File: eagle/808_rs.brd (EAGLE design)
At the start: 100 x 80 mm, 82 parts, among them IC1 TL072P, IC2 TL072P, Q74 MPF102, SW1_A LSP11, SW1_B LSP11, SW1_C LSP11, SW2_A LSP11, SW2_B LSP11, SW2_C LSP11

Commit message: gcode with well separated traces
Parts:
- moved ACCENT 4.33 mm to (21.1, 49.3)
- moved C111 3.31 mm to (18.3, 30.2), turned to 270 degrees
- moved R297 1.52 mm to (18.8, 49.5)
- moved SW1_C 1.44 mm to (75.9, 72.1)
- moved SW1_B 1.37 mm to (81.8, 35.6)
- moved SW2_C 0.92 mm to (82.0, 42.4)
- moved R323 0.92 mm to (77.0, 59.2)
- moved R324 0.80 mm to (76.7, 67.6)
- moved R330 0.80 mm to (85.9, 67.6)
- moved U$1 0.57 mm to (40.1, 9.14)
- moved D63 0.51 mm to (57.9, 57.1)
- moved R325 0.51 mm to (66.0, 51.6)
- moved D64 0.25 mm to (36.8, 46.7)
- moved C114 0.25 mm to (19.3, 36.8)
- moved R303 0.25 mm to (39.4, 52.3)
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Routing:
- net N$351: track 319.1 -> 324.5 mm
- net N$4: track 12.5 -> 8.40 mm
- net N$348: track 59.1 -> 62.1 mm
- net -12V: track 323.6 -> 325.9 mm
- net N$163: track 62.0 -> 64.2 mm
- net N$345: track 3.81 -> 2.59 mm
- net RS: track 2.54 -> 3.61 mm
- net N$167: track 64.0 -> 63.1 mm
- net N$473: track 3.07 -> 2.18 mm
- net N$336: track 15.5 -> 14.7 mm
- net N$170: track 73.2 -> 73.9 mm
- net GND: track 357.2 -> 358.0 mm
- net N$318: track 23.7 -> 24.4 mm
- net N$172: track 19.7 -> 19.0 mm
- net N$357: track 86.0 -> 86.7 mm
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
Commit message: schematic updated
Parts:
- removed C5: 0.1uF, TR808clone:C035-025X75
- removed D1: 1N4148DO35-7, TR808clone:DO35-7
- removed R1: 22K, TR808clone:0207/5V
- removed R295: 1K, TR808clone:0207/5V
- removed SW1_A, SW1_B, SW1_C, SW2_A, SW2_B, SW2_C: LSP11, solpad:LSP11
- added OUT_NORM: 22-23-2021, con-molex:22-23-2021
- added R238: 1K, TR808clone:0207/7
- added SW8: 808_LT_MSS42_SW_4PDT, 808_lt:808_LT_MSS42_SW_SLIDE
- OUTPUT: value LSP11 -> AUDIO-JACK; device solpad:LSP11 -> erthenvar:ERTHENVAR-JACK-90DEG
- Q59, Q61, Q62, Q63: value (none) -> 2N3904; device transistor:TO92-CBE -> 808_lt:TO92
- Q60: value (none) -> 2N3906; device transistor:TO92-EBC -> 808_lt:TO92
- moved OUTPUT 125.8 mm to (1.78, -45.0)
- moved ACCENT 23.1 mm to (20.3, 72.4)
- moved TRIGGER 23.1 mm to (21.1, 49.3)
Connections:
- removed net N$345: R319.2, SW1_B.MP
- removed net N$473: R324.1, SW1_C.MP
- removed net RS_CL_OUT: OUTPUT.MP, R295.1
- new net LT_LC_OUT: OUTPUT.P$3, R238.1
- new net N$7: C125.P$1, SW8.P$11
- net +12V: now also Q63.1; no longer Q63.C
- net -12V: now also Q61.3; no longer Q61.E
- net GND: now also OUTPUT.P$1, OUT_NORM.2, Q59.3, Q62.3; no longer Q59.E, Q62.E, R1.1
- net N$161: now also Q61.1; no longer Q61.C
- net N$163: now also Q61.2; no longer Q61.B
- net N$165: now also SW8.P$3; no longer SW2_B.MP
- net N$170: now also R238.2; no longer R295.2
- net N$172: now also Q62.1; no longer Q62.C
- net N$174: now also Q62.2; no longer Q62.B
- net N$2: now also R319.2, SW8.P$10; no longer C125.P$1, SW1_A.MP
- net N$306: now also SW8.P$1; no longer SW2_C.MP
- net N$317: now also Q60.2; no longer Q60.B
- net N$318: now also Q59.2; no longer Q59.B
- net N$319: now also Q59.1; no longer Q59.C
- net N$329: now also Q63.2; no longer Q63.B
- net N$330: now also Q63.3; no longer Q63.E
- net N$338: now also SW8.P$2; no longer SW2_A.MP
- net N$357: now also Q60.1; no longer Q60.C
- net N$5: now also OUTPUT.P$2, OUT_NORM.1; no longer D1.A, TRIGGER.MP
- net N$6: now also R324.1, SW8.P$12; no longer C5.P$1, D1.C, R1.2
- net RS: now also TRIGGER.MP, U$1.15, U$1.16; no longer ACCENT.MP
- net TRIG: now also ACCENT.MP, Q60.3, U$1.13, U$1.14; no longer C5.P$2, Q60.E
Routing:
- net N$6: track 10.7 -> 0.00 mm
- net RS_CL_OUT: track 8.89 -> 0.00 mm
- net GND: track 358.0 -> 364.8 mm
- net N$317: track 13.8 -> 19.5 mm
- net -12V: track 325.9 -> 331.2 mm
- net TRIG: track 12.6 -> 7.62 mm
- net N$161: track 67.4 -> 72.3 mm
- net N$5: track 4.86 -> 0.00 mm
- net N$170: track 73.9 -> 69.3 mm
- net N$319: track 4.31 -> 8.08 mm
- net N$172: track 19.0 -> 22.8 mm
- net +12V: track 132.2 -> 136.0 mm
- net N$2: track 3.27 -> 0.00 mm
- net N$329: track 24.8 -> 28.0 mm
- net N$345: track 2.59 -> 0.00 mm
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
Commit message: 2sk30
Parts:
- removed Q74: MPF102, mes_transistors:TO92F
- added Q1: 2SK30, 808:TO92
- moved R330 171.8 mm to (-85.1, 85.1), turned to 0 degrees
- moved R326 169.6 mm to (-69.8, 85.1)
- moved R318 167.9 mm to (-85.1, 78.7), turned to 0 degrees
- moved R327 157.7 mm to (-77.5, 85.1), turned to 0 degrees
- moved Q62 147.8 mm to (-80.0, 90.2), turned to 0 degrees
- moved R316 143.2 mm to (-69.8, 78.7), turned to 0 degrees
- moved R317 143.1 mm to (-77.5, 78.7), turned to 0 degrees
- moved R314 140.4 mm to (-54.6, 78.7), turned to 0 degrees
- moved C117 138.7 mm to (-76.2, 40.6), turned to 0 degrees
- moved C116 134.8 mm to (-69.8, 40.6), turned to 0 degrees
- moved C126 132.6 mm to (-34.3, 66.0)
- moved R325 132.6 mm to (-62.2, 85.1), turned to 0 degrees
- moved R324 132.5 mm to (-54.6, 85.1), turned to 0 degrees
- moved R313 128.9 mm to (-47.0, 78.7), turned to 0 degrees
- moved R323 126.6 mm to (-47.0, 85.1), turned to 0 degrees
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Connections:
- removed net N$170: C153.2, IC2.7, Q74.1, R238.2, R327.1, R330.2, VR16.2
- new net N$8: C153.2, IC2.7, Q1.1, R238.2, R327.1, R330.2, VR16.2
- net N$161: now also Q1.2; no longer Q74.3
- net N$351: now also Q1.3; no longer Q74.2
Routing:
- net GND: track 364.8 -> 0.00 mm
- net -12V: track 331.2 -> 0.00 mm
- net N$351: track 324.5 -> 0.00 mm
- net +12V: track 136.0 -> 0.00 mm, vias 2 -> 0
- net N$357: track 87.6 -> 0.00 mm
- net N$161: track 72.3 -> 0.00 mm, vias 2 -> 0
- net N$170: track 69.3 -> 0.00 mm
- net N$340: track 69.1 -> 0.00 mm, vias 2 -> 0
- net N$163: track 66.0 -> 0.00 mm
- net N$167: track 63.1 -> 0.00 mm
- net N$348: track 62.1 -> 0.00 mm
- net N$339: track 47.2 -> 0.00 mm
- net N$333: track 44.8 -> 0.00 mm, vias 2 -> 0
- net N$330: track 36.9 -> 0.00 mm
- net N$352: track 30.7 -> 0.00 mm
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
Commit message: more placement
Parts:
- moved Q62 138.7 mm to (55.9, 62.2), turned to 90 degrees
- moved C116 114.3 mm to (44.5, 38.1), turned to 180 degrees
- moved Q1 105.4 mm to (12.7, 35.6), turned to 180 degrees
- moved C113 102.7 mm to (19.1, 36.8), turned to 90 degrees
- moved R320 99.7 mm to (45.7, 14.0), turned to 180 degrees
- moved C120 94.1 mm to (49.5, 62.2), turned to 270 degrees
- moved R309 91.9 mm to (45.7, 19.1), turned to 180 degrees
- moved D62 89.6 mm to (47.0, 48.3), turned to 180 degrees
- moved C111 89.2 mm to (38.1, 48.3)
- moved R300 74.0 mm to (39.4, 52.1), turned to 180 degrees
- moved R322 73.9 mm to (27.9, 54.6)
- moved R321 71.1 mm to (35.6, 62.2)
- moved D61 67.4 mm to (43.2, 55.9), turned to 180 degrees
- moved C126 64.8 mm to (19.1, 29.2), turned to 90 degrees
- moved R299 64.3 mm to (39.4, 62.2), turned to 90 degrees
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
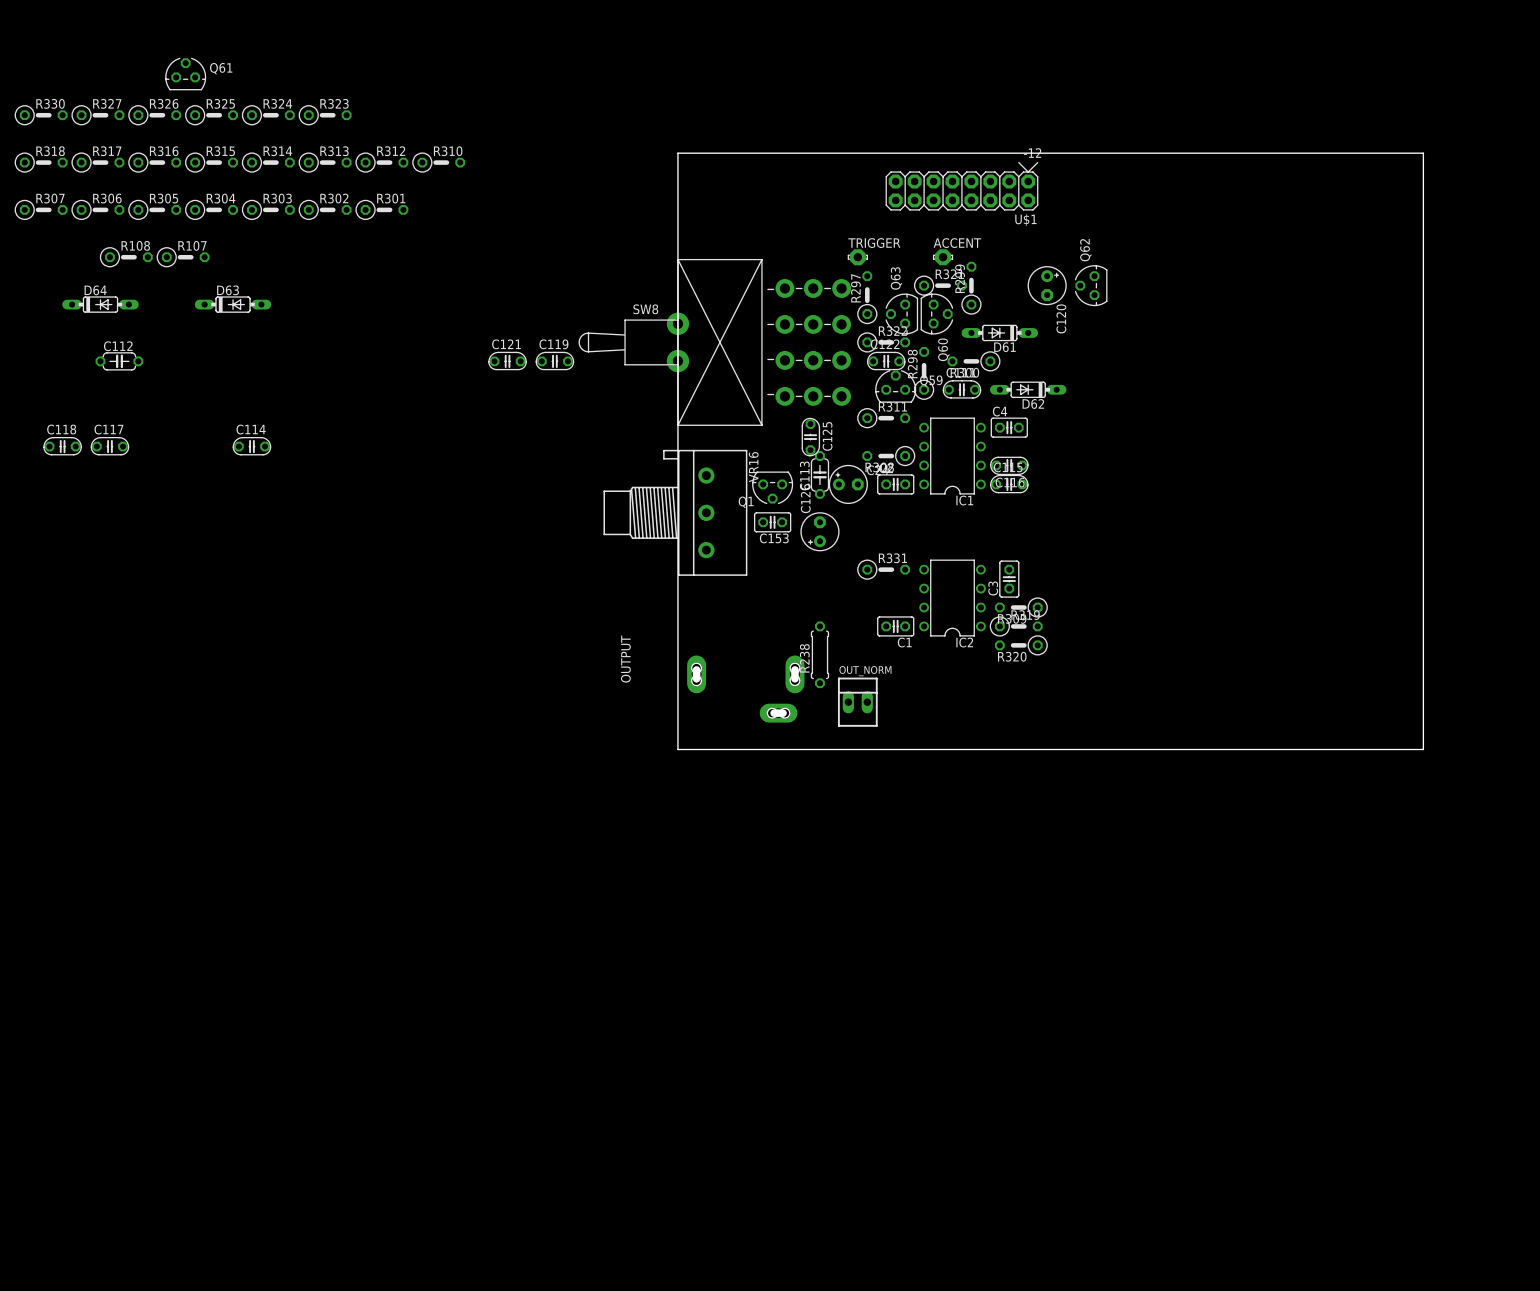
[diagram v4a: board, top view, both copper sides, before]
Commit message: restarted layout with care
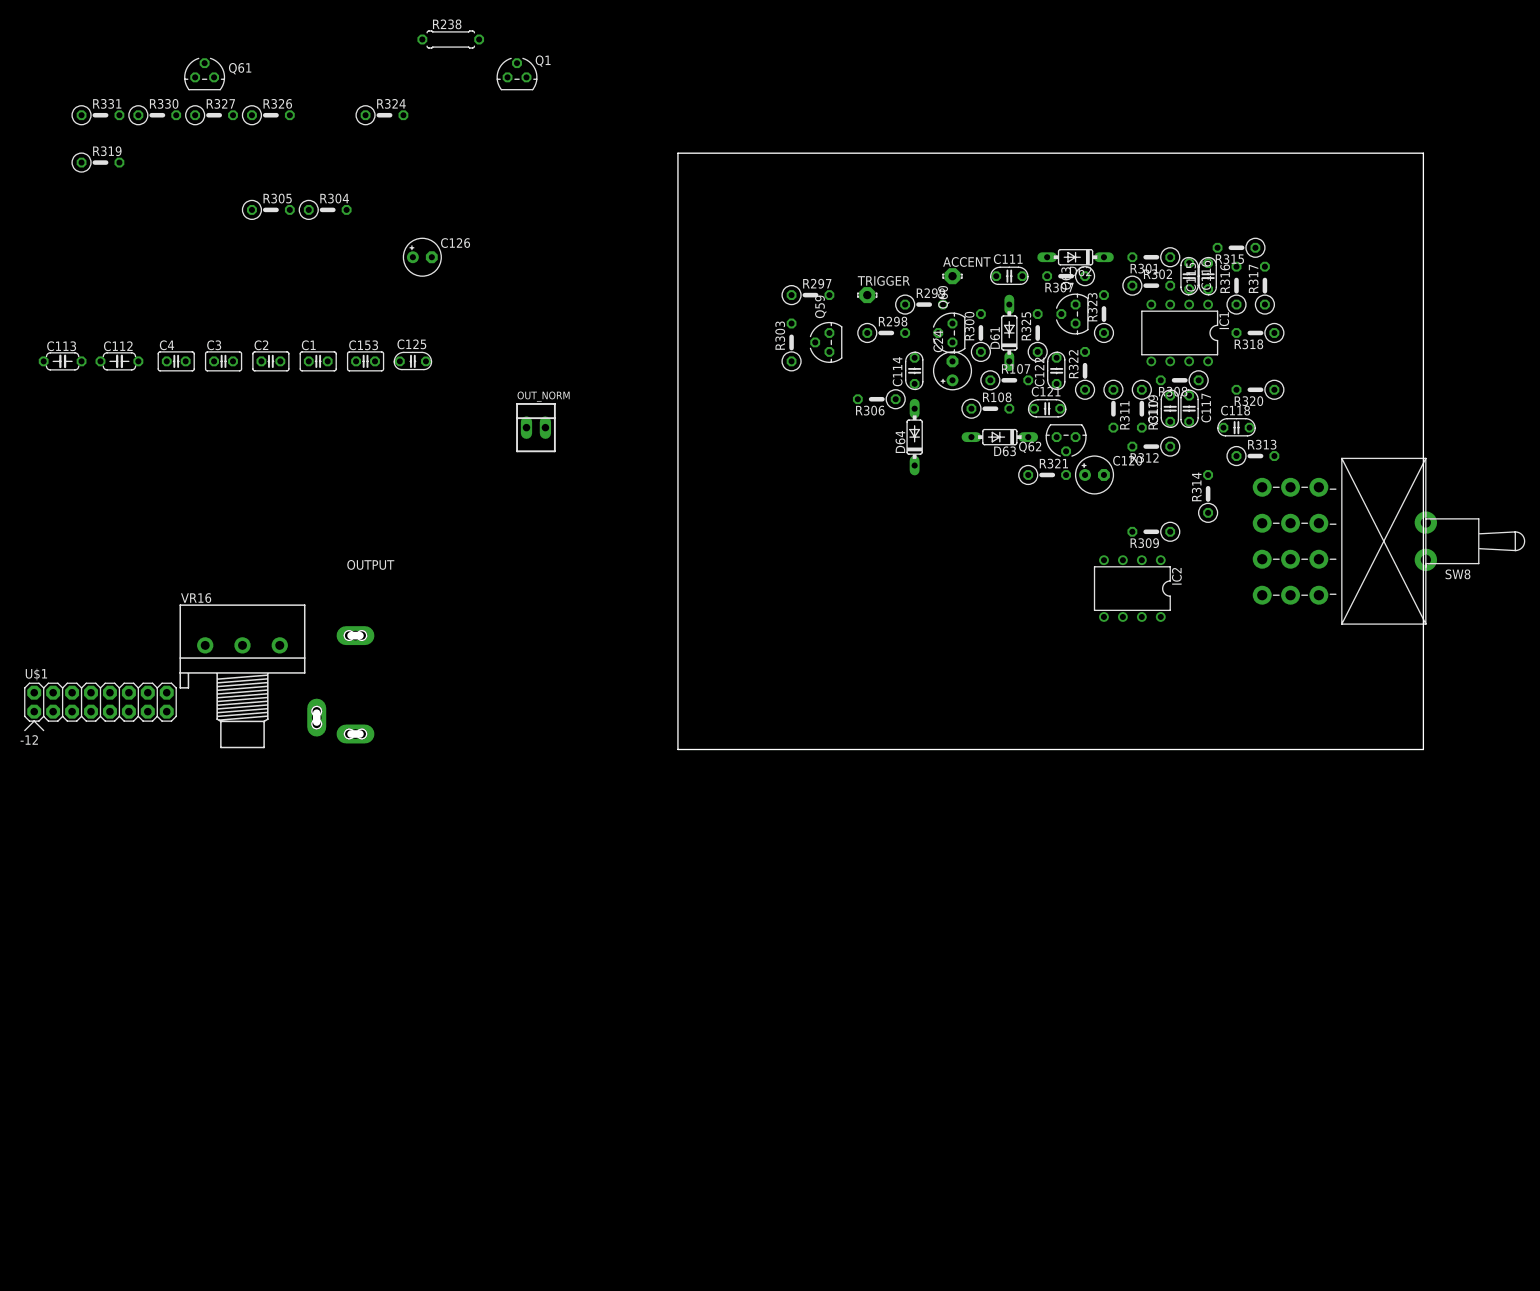
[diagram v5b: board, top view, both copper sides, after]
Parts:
- moved R318 164.2 mm to (77.5, 55.9), turned to 180 degrees
- moved C118 157.5 mm to (74.9, 43.2)
- moved R317 157.1 mm to (78.7, 62.2), turned to 90 degrees
- moved R316 145.7 mm to (74.9, 62.2), turned to 90 degrees
- moved C117 144.9 mm to (68.6, 45.7), turned to 270 degrees
- moved U$1 138.8 mm to (-80.0, 6.35), turned to 0 degrees
- moved R319 138.0 mm to (-77.5, 78.7)
- moved R315 137.6 mm to (74.9, 67.3), turned to 180 degrees
- moved R307 137.4 mm to (52.1, 63.5), turned to 180 degrees
- moved R314 133.4 mm to (71.1, 34.3), turned to 90 degrees
- moved R313 130.5 mm to (77.5, 39.4)
- moved R331 121.8 mm to (-77.5, 85.1)
- moved R108 117.3 mm to (41.9, 45.7)
- moved R325 114.3 mm to (48.3, 55.9), turned to 90 degrees
- moved C4 112.1 mm to (-67.3, 52.1)
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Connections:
- net N$165: now also SW8.P$10; no longer SW8.P$3
- net N$2: now also C125.P$1, SW8.P$2; no longer R319.2, SW8.P$10
- net N$306: now also SW8.P$12; no longer SW8.P$1
- net N$338: now also SW8.P$11; no longer SW8.P$2
- net N$6: now also SW8.P$1; no longer SW8.P$12
- net N$7: now also R319.2, SW8.P$3; no longer C125.P$1, SW8.P$11

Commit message: placed parts manually
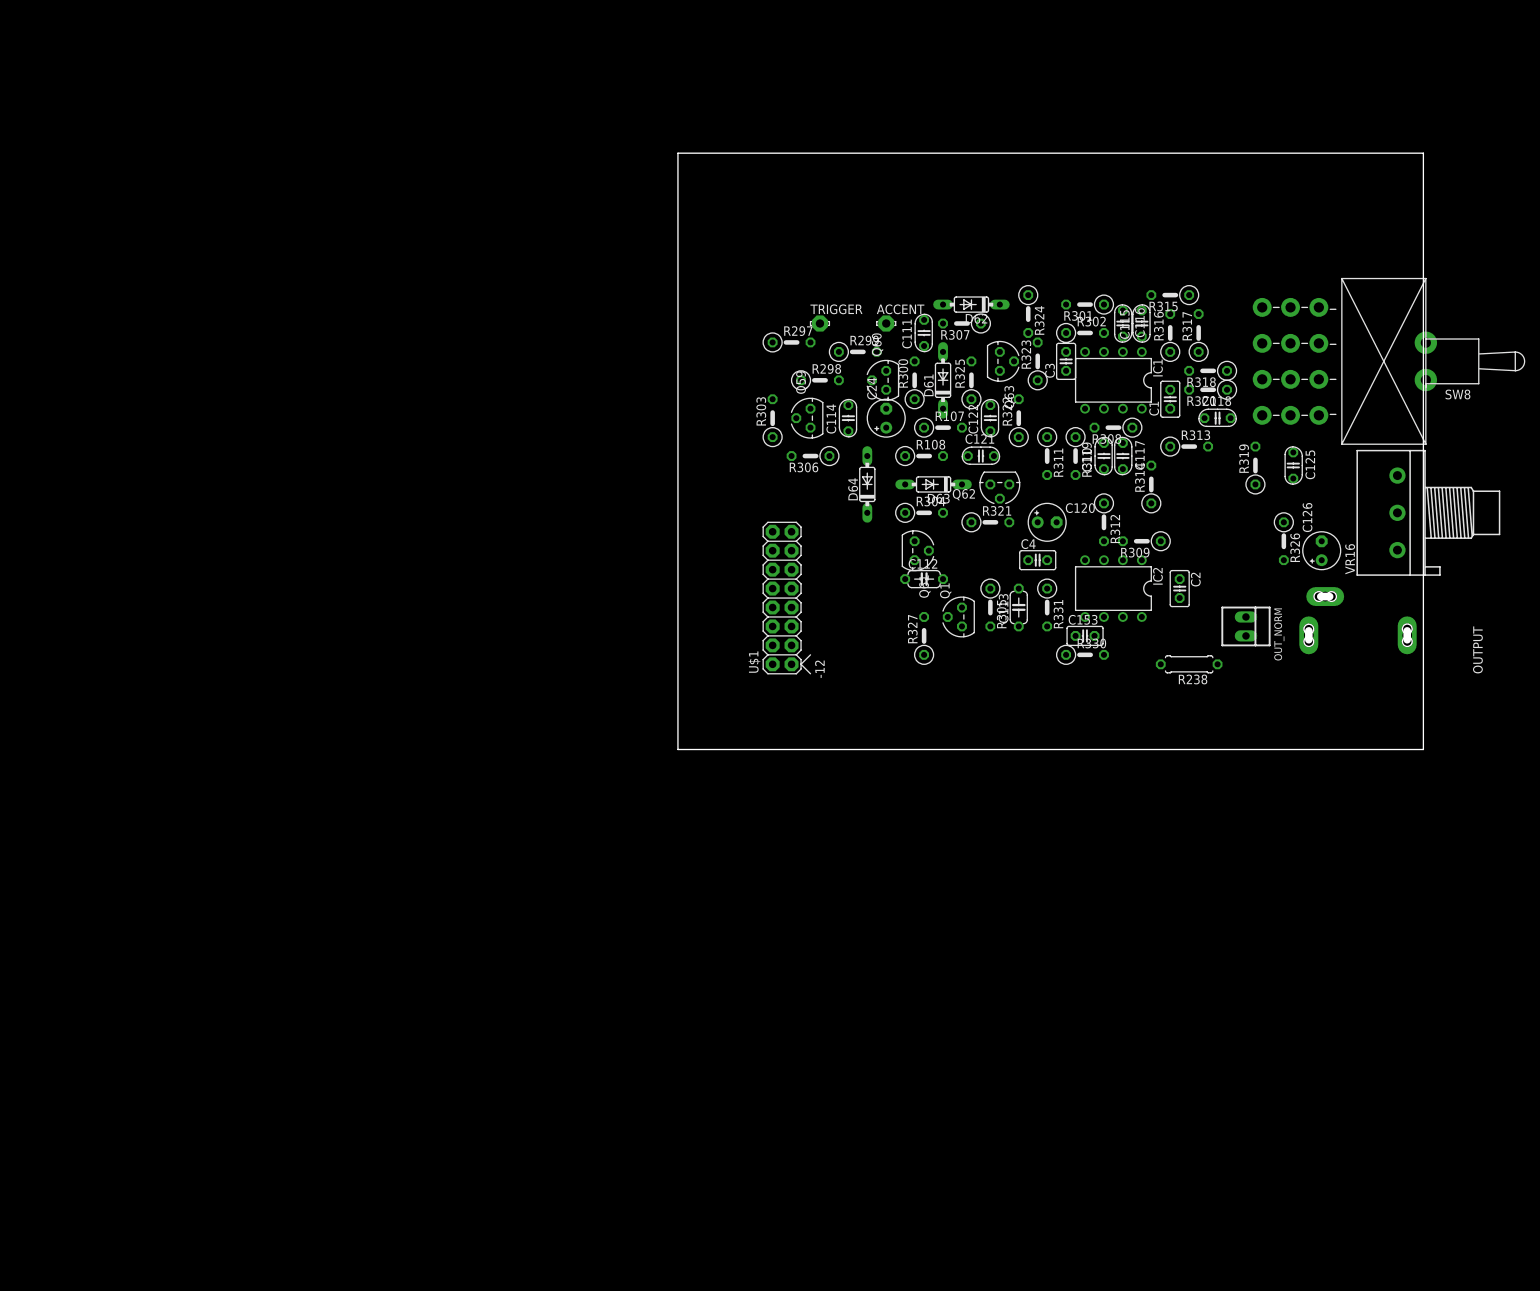
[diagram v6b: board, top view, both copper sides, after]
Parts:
- moved R319 160.2 mm to (77.5, 38.1), turned to 90 degrees
- moved VR16 156.0 mm to (96.5, 31.8), turned to 90 degrees
- moved OUTPUT 148.6 mm to (100.3, 20.3), turned to 270 degrees
- moved R326 147.4 mm to (81.3, 27.9), turned to 270 degrees
- moved R330 144.0 mm to (54.6, 12.7)
- moved R331 143.1 mm to (49.5, 19.1), turned to 270 degrees
- moved C113 132.5 mm to (45.7, 19.1), turned to 90 degrees
- moved R238 129.8 mm to (68.6, 11.4), turned to 180 degrees
- moved C126 126.9 mm to (86.4, 26.7), turned to 90 degrees
- moved C2 125.7 mm to (67.3, 21.6), turned to 270 degrees
- moved C125 118.9 mm to (82.5, 38.1), turned to 270 degrees
- moved C4 118.6 mm to (48.3, 25.4)
- moved R327 118.1 mm to (33.0, 15.2), turned to 90 degrees
- moved Q61 114.5 mm to (31.8, 26.7), turned to 270 degrees
- moved C1 114.4 mm to (66.0, 47.0), turned to 90 degrees
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
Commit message: working up to route
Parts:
- moved R311 4.58 mm to (53.3, 36.8)
- moved R313 4.58 mm to (72.4, 38.1)
- moved R327 4.58 mm to (30.5, 11.4), turned to 180 degrees
- moved R330 4.58 mm to (58.4, 10.2)
- moved C153 4.02 mm to (58.4, 14.0)
- moved Q1 4.02 mm to (34.3, 16.5)
- moved Q60 4.02 mm to (24.1, 50.8)
- moved R315 4.02 mm to (69.8, 59.7)
- moved R316 4.02 mm to (69.8, 54.6)
- moved C118 3.59 mm to (69.8, 41.9)
- moved R322 3.59 mm to (48.3, 41.9)
- moved ACCENT 3.59 mm to (25.4, 59.7)
- moved R305 3.59 mm to (39.4, 16.5)
- moved R317 2.84 mm to (72.4, 54.6)
- moved C112 2.84 mm to (31.8, 20.3)
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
